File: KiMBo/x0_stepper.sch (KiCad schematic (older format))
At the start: 25 parts, among them U19 TMC2130

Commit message: Assocate more footprints
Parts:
- C101, C102: footprint Capacitors_SMD:C_0402 -> Capacitors_SMD:C_0603
- R138, R139, R140, R141, R142, R143: footprint (none) -> Resistors_SMD:R_0603
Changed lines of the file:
@@
 F 0 "C102" H 9265 4196 50  0000 L CNN
 F 1 "22nF" H 9265 4105 50  0000 L CNN
-F 2 "Capacitors_SMD:C_0402" H 9188 4000 50  0001 C CNN
+F 2 "Capacitors_SMD:C_0603" H 9188 4000 50  0001 C CNN
 F 3 "" H 9150 4150 50  0000 C CNN
 	1    9150 4150
@@
 F 0 "R141" V 7200 3750 50  0000 C CNN
 F 1 "2.2Ω" V 7300 3750 50  0000 C CNN
-F 2 "" V 7230 3750 50  0001 C CNN
+F 2 "Resistors_SMD:R_0603" V 7230 3750 50  0001 C CNN
 F 3 "" H 7300 3750 50  0000 C CNN
 	1    7300 3750
@@
 F 0 "R139" H 6119 4296 50  0000 L CNN
 F 1 "4.7kΩ" H 6119 4205 50  0000 L CNN
-F 2 "" V 5980 4250 50  0001 C CNN
+F 2 "Resistors_SMD:R_0603" V 5980 4250 50  0001 C CNN
 F 3 "" H 6050 4250 50  0000 C CNN
 	1    6050 4250
@@
 F 0 "C101" H 7550 4050 50  0000 L CNN
 F 1 "4.7μF" H 7550 3850 50  0000 L CNN
-F 2 "Capacitors_SMD:C_0402" H 7538 3800 50  0001 C CNN
+F 2 "Capacitors_SMD:C_0603" H 7538 3800 50  0001 C CNN
 F 3 "" H 7500 3950 50  0000 C CNN
 	1    7500 3950
@@
 F 0 "R142" H 9319 6746 50  0000 L CNN
 F 1 "5.23kΩ" H 9319 6655 50  0000 L CNN
-F 2 "" V 9180 6700 50  0001 C CNN
+F 2 "Resistors_SMD:R_0603" V 9180 6700 50  0001 C CNN
 F 3 "" H 9250 6700 50  0000 C CNN
 	1    9250 6700
@@
 F 0 "R143" V 9250 6900 50  0000 C CNN
 F 1 "4.75kΩ" V 9350 6900 50  0000 C CNN
-F 2 "" V 9380 6900 50  0001 C CNN
+F 2 "Resistors_SMD:R_0603" V 9380 6900 50  0001 C CNN
 F 3 "" H 9450 6900 50  0000 C CNN
 	1    9450 6900
@@
 F 0 "R140" H 6469 4296 50  0000 L CNN
 F 1 "4.7kΩ" H 6469 4205 50  0000 L CNN
-F 2 "" V 6330 4250 50  0001 C CNN
+F 2 "Resistors_SMD:R_0603" V 6330 4250 50  0001 C CNN
 F 3 "" H 6400 4250 50  0000 C CNN
 	1    6400 4250
@@
 F 0 "R138" H 5769 4296 50  0000 L CNN
 F 1 "4.7kΩ" H 5769 4205 50  0000 L CNN
-F 2 "" V 5630 4250 50  0001 C CNN
+F 2 "Resistors_SMD:R_0603" V 5630 4250 50  0001 C CNN
 F 3 "" H 5700 4250 50  0000 C CNN
 	1    5700 4250

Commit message: More footprint association
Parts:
- R144, R145: footprint (none) -> Resistors_SMD:R_0805
- U19: footprint (none) -> KiMBo:QFN36_5X6
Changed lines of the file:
@@
 $EndComp
 $Comp
-L GND #PWR0202
+L GND #PWR0203
 U 1 1 58C092D2
 P 7500 3300
-F 0 "#PWR0202" H 7500 3050 50  0001 C CNN
+F 0 "#PWR0203" H 7500 3050 50  0001 C CNN
 F 1 "GND" H 7500 3150 50  0000 C CNN
 F 2 "" H 7500 3300 50  0000 C CNN
@@
 $EndComp
 $Comp
-L GND #PWR0203
+L GND #PWR0204
 U 1 1 5BA7E141
 P 10350 3350
-F 0 "#PWR0203" H 10350 3100 50  0001 C CNN
+F 0 "#PWR0204" H 10350 3100 50  0001 C CNN
 F 1 "GND" H 10355 3177 50  0000 C CNN
 F 2 "" H 10350 3350 50  0000 C CNN
@@
 $EndComp
 $Comp
-L +24V #PWR0204
+L +24V #PWR0205
 U 1 1 58C092E5
 P 8550 2850
-F 0 "#PWR0204" H 8550 2700 50  0001 C CNN
+F 0 "#PWR0205" H 8550 2700 50  0001 C CNN
 F 1 "+24V" H 8565 3023 50  0000 C CNN
 F 2 "" H 8550 2850 50  0000 C CNN
@@
 F 0 "R145" H 10700 6650 50  0000 R CNN
 F 1 "220mΩ" H 10700 6750 50  0000 R CNN
-F 2 "" V 10680 6700 50  0001 C CNN
+F 2 "Resistors_SMD:R_0805" V 10680 6700 50  0001 C CNN
 F 3 "" H 10750 6700 50  0000 C CNN
 	1    10750 6700
@@
 F 0 "R144" H 9900 6650 50  0000 R CNN
 F 1 "220mΩ" H 9900 6750 50  0000 R CNN
-F 2 "" V 9880 6700 50  0001 C CNN
+F 2 "Resistors_SMD:R_0805" V 9880 6700 50  0001 C CNN
 F 3 "" H 9950 6700 50  0000 C CNN
 	1    9950 6700
@@
 $EndComp
 $Comp
-L GND #PWR0205
+L GND #PWR0206
 U 1 1 5BA7E146
 P 9650 7050
-F 0 "#PWR0205" H 9650 6800 50  0001 C CNN
+F 0 "#PWR0206" H 9650 6800 50  0001 C CNN
 F 1 "GND" H 9655 6877 50  0000 C CNN
 F 2 "" H 9650 7050 50  0000 C CNN
@@
 NoConn ~ 7700 5700
 $Comp
-L GND #PWR0206
+L GND #PWR0207
 U 1 1 5BA7E149
 P 7650 6100
-F 0 "#PWR0206" H 7650 5850 50  0001 C CNN
+F 0 "#PWR0207" H 7650 5850 50  0001 C CNN
 F 1 "GND" H 7655 5927 50  0000 C CNN
 F 2 "" H 7650 6100 50  0000 C CNN
@@
 $EndComp
 $Comp
-L GND #PWR0207
+L GND #PWR0208
 U 1 1 58C0936A
 P 9250 5200
-F 0 "#PWR0207" H 9250 4950 50  0001 C CNN
+F 0 "#PWR0208" H 9250 4950 50  0001 C CNN
 F 1 "GND" H 9250 5050 50  0000 C CNN
 F 2 "" H 9250 5200 50  0000 C CNN
@@
 $EndComp
 $Comp
-L GND #PWR0208
+L GND #PWR0209
 U 1 1 58C0937E
 P 9250 6050
-F 0 "#PWR0208" H 9250 5800 50  0001 C CNN
+F 0 "#PWR0209" H 9250 5800 50  0001 C CNN
 F 1 "GND" H 9250 5900 50  0000 C CNN
 F 2 "" H 9250 6050 50  0000 C CNN
@@
 F 0 "U19" H 7950 6200 60  0000 C CNN
 F 1 "TMC2130" H 8700 6200 60  0000 C CNN
-F 2 "" H 8400 5000 60  0001 C CNN
+F 2 "KiMBo:QFN36_5X6" H 8400 5000 60  0001 C CNN
 F 3 "" H 8400 5000 60  0000 C CNN
 	1    8400 4700
@@
 	5700 3500 7700 3500
 $Comp
-L VDD_3V3B #PWR0209
+L VDD_3V3B #PWR0210
 U 1 1 5A2FF856
 P 6750 3450
-F 0 "#PWR0209" H 6750 3300 50  0001 C CNN
+F 0 "#PWR0210" H 6750 3300 50  0001 C CNN
 F 1 "VDD_3V3B" H 6765 3623 50  0000 C CNN
 F 2 "" H 6750 3450 50  0000 C CNN

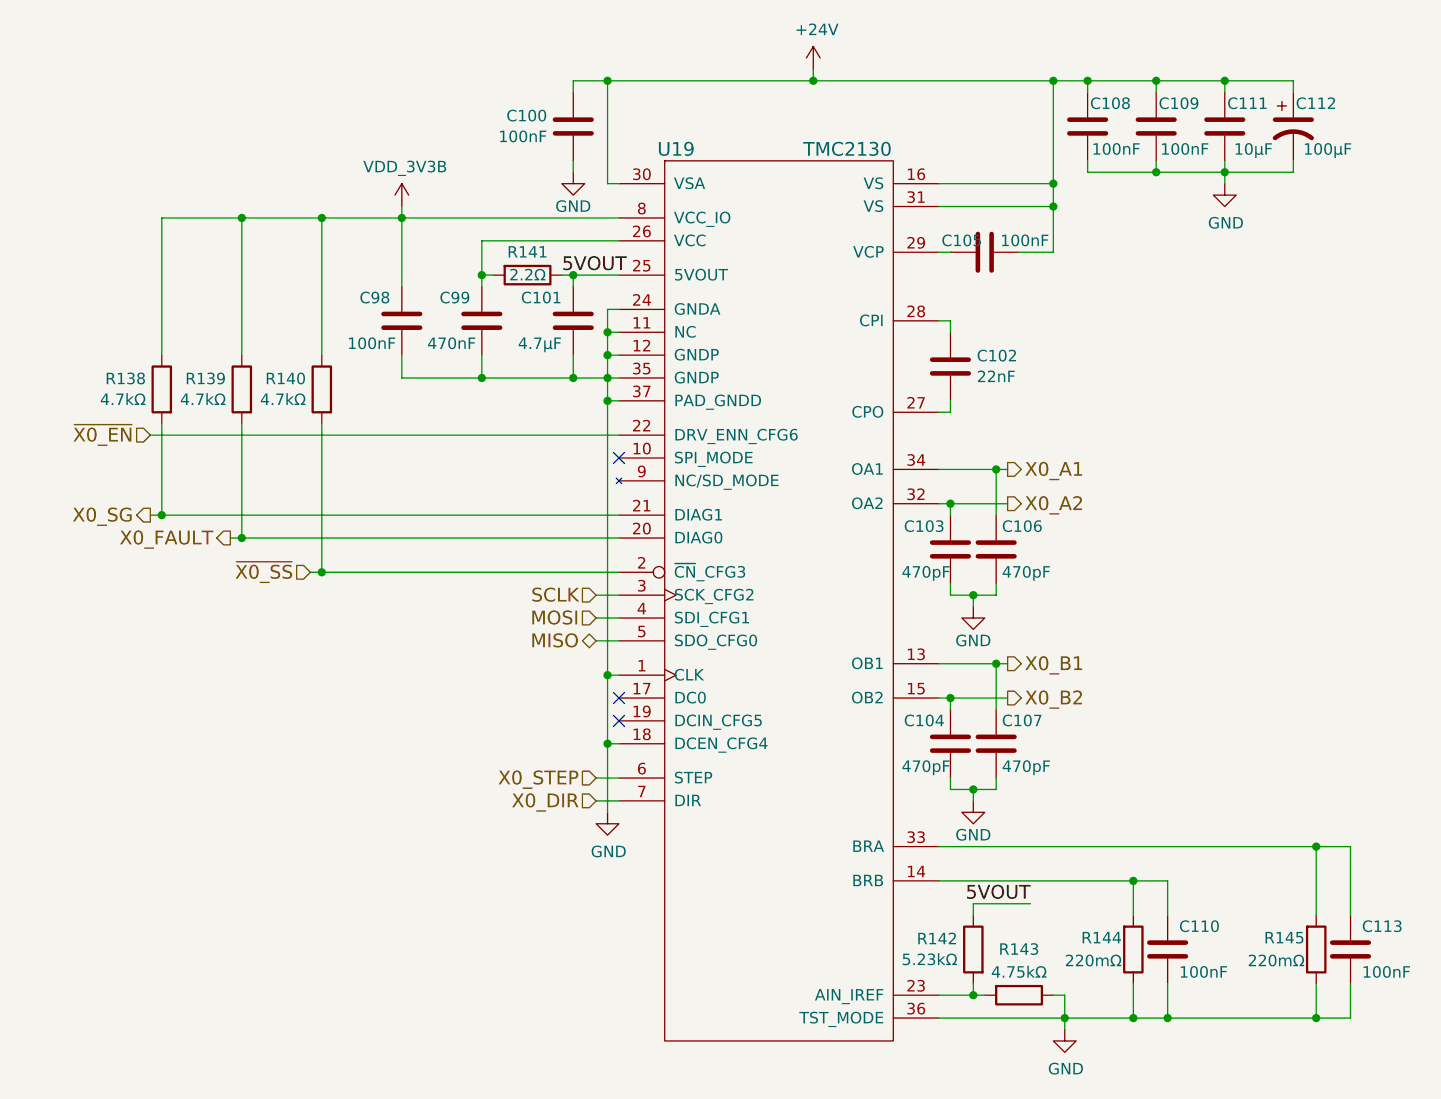
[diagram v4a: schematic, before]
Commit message: Add more footprints and more associations, one association left!
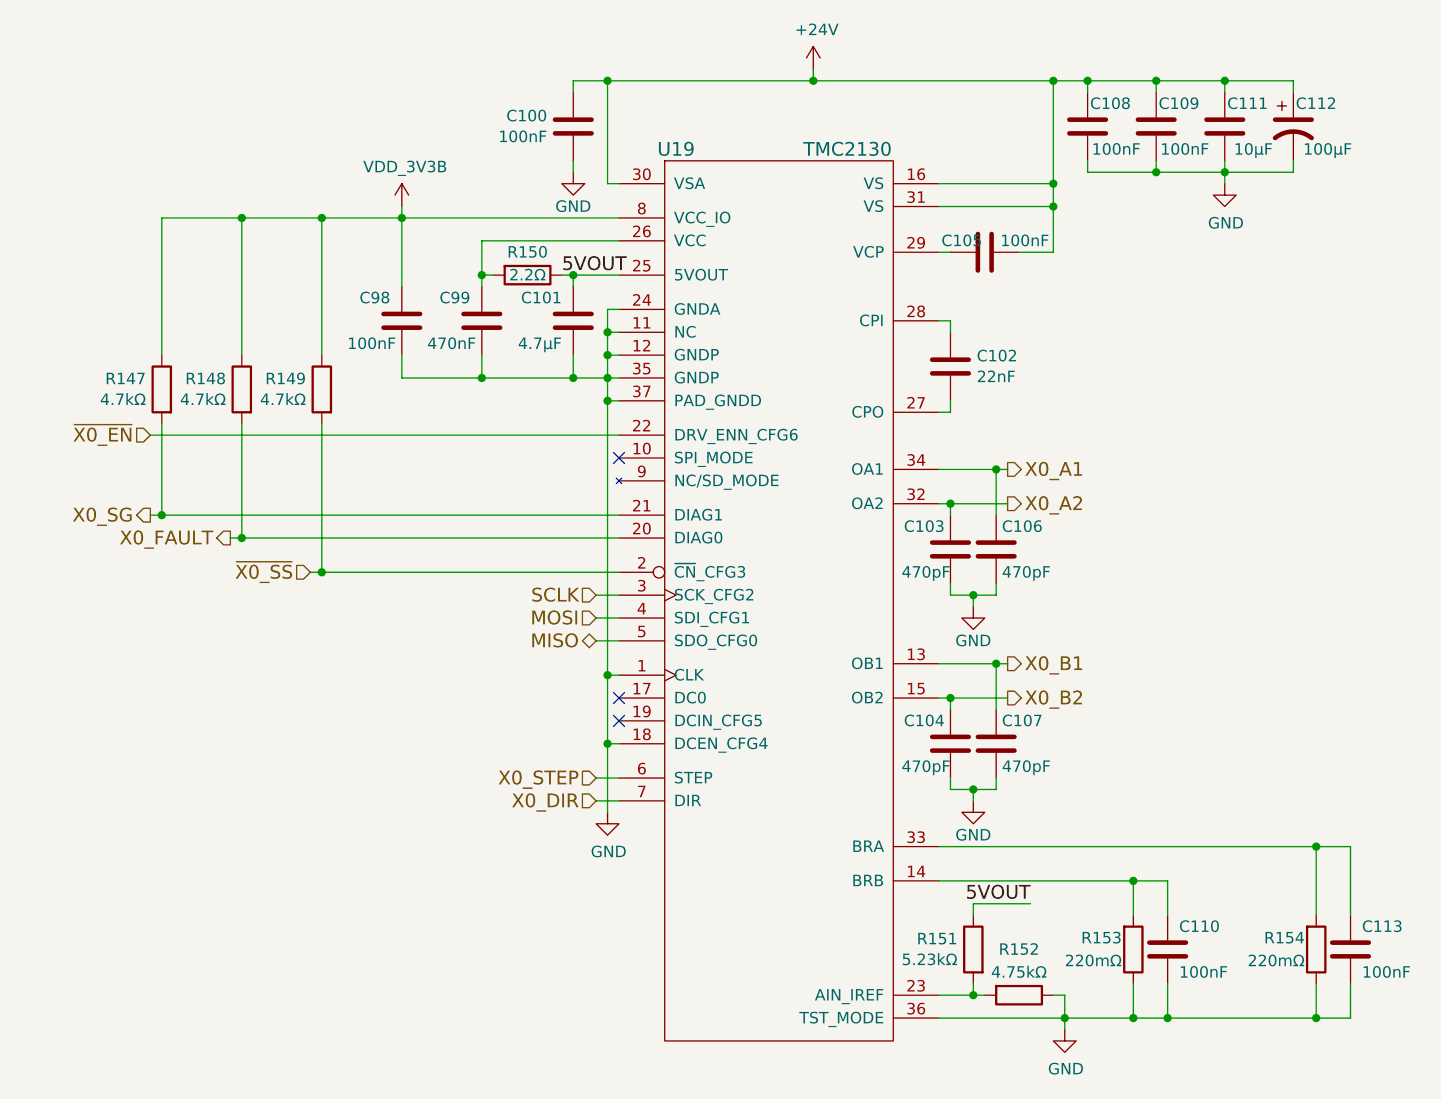
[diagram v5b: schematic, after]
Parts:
- R152: renamed from R143; footprint Resistors_SMD:R_0603 -> Resistors_SMD:R_0805
- R154: renamed from R145; footprint Resistors_SMD:R_0805 -> Resistors_SMD:R_0603
- renumbered R138 to R147, R139 to R148, R140 to R149, R141 to R150, R142 to R151, R144 to R153
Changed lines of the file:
@@
 $EndComp
 $Comp
-L GND #PWR0203
+L GND #PWR0205
 U 1 1 58C092D2
 P 7500 3300
-F 0 "#PWR0203" H 7500 3050 50  0001 C CNN
+F 0 "#PWR0205" H 7500 3050 50  0001 C CNN
 F 1 "GND" H 7500 3150 50  0000 C CNN
 F 2 "" H 7500 3300 50  0000 C CNN
@@
 $EndComp
 $Comp
-L GND #PWR0204
+L GND #PWR0206
 U 1 1 5BA7E141
 P 10350 3350
-F 0 "#PWR0204" H 10350 3100 50  0001 C CNN
+F 0 "#PWR0206" H 10350 3100 50  0001 C CNN
 F 1 "GND" H 10355 3177 50  0000 C CNN
 F 2 "" H 10350 3350 50  0000 C CNN
@@
 $EndComp
 $Comp
-L +24V #PWR0205
+L +24V #PWR0207
 U 1 1 58C092E5
 P 8550 2850
-F 0 "#PWR0205" H 8550 2700 50  0001 C CNN
+F 0 "#PWR0207" H 8550 2700 50  0001 C CNN
 F 1 "+24V" H 8565 3023 50  0000 C CNN
 F 2 "" H 8550 2850 50  0000 C CNN
@@
 $EndComp
 $Comp
-L R R145
+L R R154
 U 1 1 58C092F2
 P 10750 6700
-F 0 "R145" H 10700 6650 50  0000 R CNN
+F 0 "R154" H 10700 6650 50  0000 R CNN
 F 1 "220mΩ" H 10700 6750 50  0000 R CNN
-F 2 "Resistors_SMD:R_0805" V 10680 6700 50  0001 C CNN
+F 2 "Resistors_SMD:R_0603" V 10680 6700 50  0001 C CNN
 F 3 "" H 10750 6700 50  0000 C CNN
 	1    10750 6700
@@
 $EndComp
 $Comp
-L R R144
+L R R153
 U 1 1 58C092F9
 P 9950 6700
-F 0 "R144" H 9900 6650 50  0000 R CNN
+F 0 "R153" H 9900 6650 50  0000 R CNN
 F 1 "220mΩ" H 9900 6750 50  0000 R CNN
 F 2 "Resistors_SMD:R_0805" V 9880 6700 50  0001 C CNN
@@
 $EndComp
 $Comp
-L GND #PWR0206
+L GND #PWR0208
 U 1 1 5BA7E146
 P 9650 7050
-F 0 "#PWR0206" H 9650 6800 50  0001 C CNN
+F 0 "#PWR0208" H 9650 6800 50  0001 C CNN
 F 1 "GND" H 9655 6877 50  0000 C CNN
 F 2 "" H 9650 7050 50  0000 C CNN
@@
 NoConn ~ 7700 5600
 $Comp
-L R R141
+L R R150
 U 1 1 5BA7E147
 P 7300 3750
-F 0 "R141" V 7200 3750 50  0000 C CNN
+F 0 "R150" V 7200 3750 50  0000 C CNN
 F 1 "2.2Ω" V 7300 3750 50  0000 C CNN
 F 2 "Resistors_SMD:R_0603" V 7230 3750 50  0001 C CNN
@@
 NoConn ~ 7700 5700
 $Comp
-L GND #PWR0207
+L GND #PWR0209
 U 1 1 5BA7E149
 P 7650 6100
-F 0 "#PWR0207" H 7650 5850 50  0001 C CNN
+F 0 "#PWR0209" H 7650 5850 50  0001 C CNN
 F 1 "GND" H 7655 5927 50  0000 C CNN
 F 2 "" H 7650 6100 50  0000 C CNN
@@
 X0_FAULT
 $Comp
-L R R139
+L R R148
 U 1 1 58C09331
 P 6050 4250
-F 0 "R139" H 6119 4296 50  0000 L CNN
+F 0 "R148" H 6119 4296 50  0000 L CNN
 F 1 "4.7kΩ" H 6119 4205 50  0000 L CNN
 F 2 "Resistors_SMD:R_0603" V 5980 4250 50  0001 C CNN
@@
 5VOUT
 $Comp
-L R R142
+L R R151
 U 1 1 5BA7E14D
 P 9250 6700
-F 0 "R142" H 9319 6746 50  0000 L CNN
+F 0 "R151" H 9319 6746 50  0000 L CNN
 F 1 "5.23kΩ" H 9319 6655 50  0000 L CNN
 F 2 "Resistors_SMD:R_0603" V 9180 6700 50  0001 C CNN
@@
 5VOUT
 $Comp
-L R R143
+L R R152
 U 1 1 5BA7E14E
 P 9450 6900
-F 0 "R143" V 9250 6900 50  0000 C CNN
+F 0 "R152" V 9250 6900 50  0000 C CNN
 F 1 "4.75kΩ" V 9350 6900 50  0000 C CNN
-F 2 "Resistors_SMD:R_0603" V 9380 6900 50  0001 C CNN
+F 2 "Resistors_SMD:R_0805" V 9380 6900 50  0001 C CNN
 F 3 "" H 9450 6900 50  0000 C CNN
 	1    9450 6900
@@
 $EndComp
 $Comp
-L R R140
+L R R149
 U 1 1 58C09353
 P 6400 4250
-F 0 "R140" H 6469 4296 50  0000 L CNN
+F 0 "R149" H 6469 4296 50  0000 L CNN
 F 1 "4.7kΩ" H 6469 4205 50  0000 L CNN
 F 2 "Resistors_SMD:R_0603" V 6330 4250 50  0001 C CNN
@@
 $EndComp
 $Comp
-L GND #PWR0208
+L GND #PWR0210
 U 1 1 58C0936A
 P 9250 5200
-F 0 "#PWR0208" H 9250 4950 50  0001 C CNN
+F 0 "#PWR0210" H 9250 4950 50  0001 C CNN
 F 1 "GND" H 9250 5050 50  0000 C CNN
 F 2 "" H 9250 5200 50  0000 C CNN
@@
 $EndComp
 $Comp
-L GND #PWR0209
+L GND #PWR0211
 U 1 1 58C0937E
 P 9250 6050
-F 0 "#PWR0209" H 9250 5800 50  0001 C CNN
+F 0 "#PWR0211" H 9250 5800 50  0001 C CNN
 F 1 "GND" H 9250 5900 50  0000 C CNN
 F 2 "" H 9250 6050 50  0000 C CNN
@@
 	9150 6000 9150 5950
 $Comp
-L R R138
+L R R147
 U 1 1 5BA7E158
 P 5700 4250
-F 0 "R138" H 5769 4296 50  0000 L CNN
+F 0 "R147" H 5769 4296 50  0000 L CNN
 F 1 "4.7kΩ" H 5769 4205 50  0000 L CNN
 F 2 "Resistors_SMD:R_0603" V 5630 4250 50  0001 C CNN
@@
 	5700 3500 7700 3500
 $Comp
-L VDD_3V3B #PWR0210
+L VDD_3V3B #PWR0212
 U 1 1 5A2FF856
 P 6750 3450
-F 0 "#PWR0210" H 6750 3300 50  0001 C CNN
+F 0 "#PWR0212" H 6750 3300 50  0001 C CNN
 F 1 "VDD_3V3B" H 6765 3623 50  0000 C CNN
 F 2 "" H 6750 3450 50  0000 C CNN
